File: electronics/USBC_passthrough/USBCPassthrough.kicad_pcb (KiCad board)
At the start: 4 copper layers, 41 x 14 mm, 2 parts, among them J1 USB_C_Receptacle_USB2.0_16P, J2 USB_C_Receptacle_USB2.0_16P

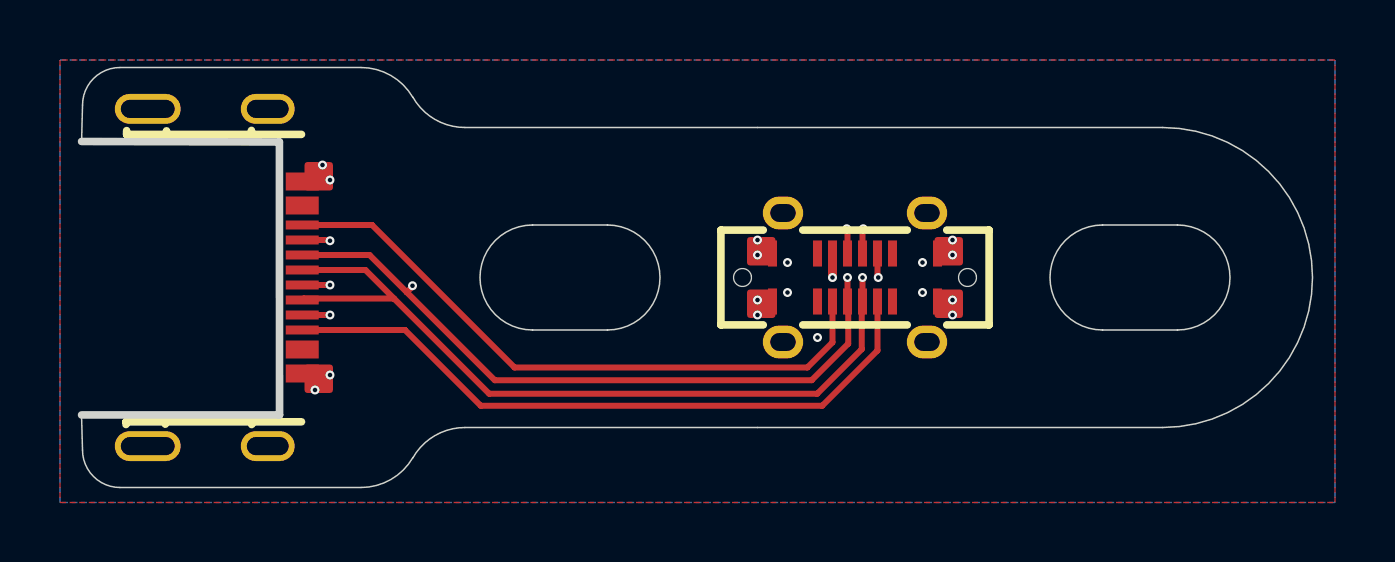
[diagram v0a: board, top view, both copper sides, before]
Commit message: fixed passthrough circuit
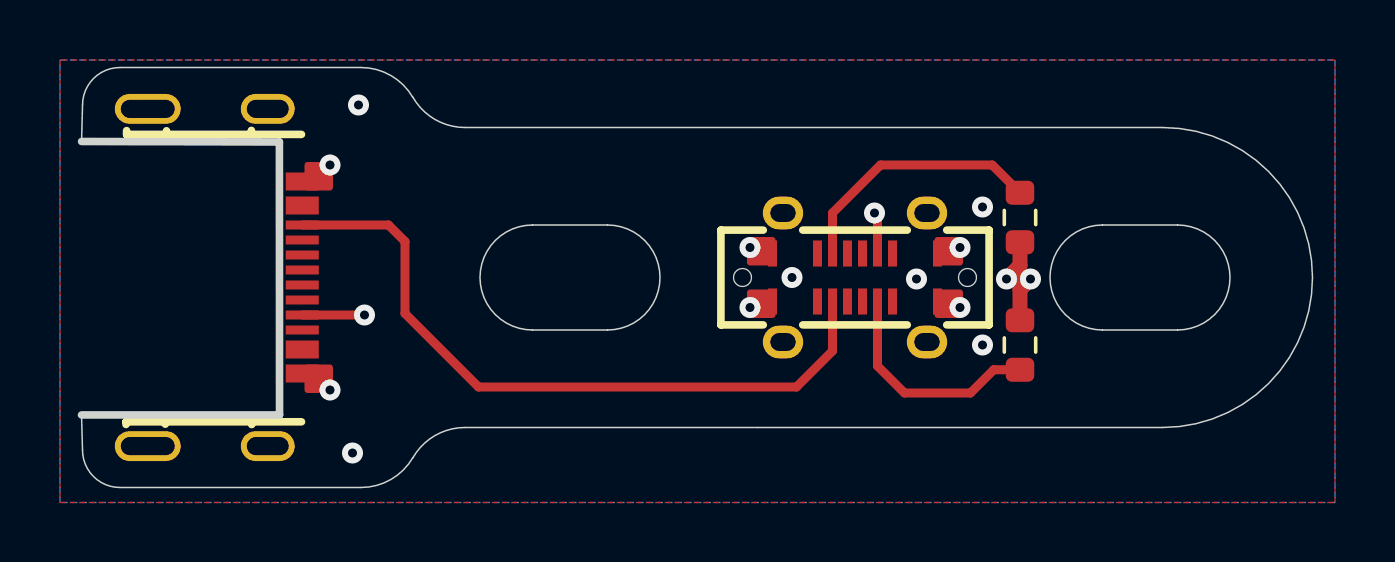
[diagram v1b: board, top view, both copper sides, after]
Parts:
- added R1: 5k1, Resistor_SMD:R_0603_1608Metric, F.Cu at (158.2, 97.0)
- added R2: 5k1, Resistor_SMD:R_0603_1608Metric, F.Cu at (158.2, 92.8)
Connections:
- J1 pad A6: Net-(J1-D+-PadA6) -> unconnected-(J1-D+-PadA6)
- J1 pad A7: Net-(J1-D--PadA7) -> unconnected-(J1-D--PadA7)
- J1 pad B6: Net-(J1-D+-PadA6) -> unconnected-(J1-D+-PadB6)
- J1 pad B7: Net-(J1-D--PadA7) -> unconnected-(J1-D--PadB7)
- J2 pad A5: Net-(J1-CC1) -> unconnected-(J2-CC1-PadA5)
- J2 pad A6: Net-(J1-D+-PadA6) -> unconnected-(J2-D+-PadA6)
- J2 pad A7: Net-(J1-D--PadA7) -> unconnected-(J2-D--PadA7)
- J2 pad B5: Net-(J1-CC2) -> unconnected-(J2-CC2-PadB5)
- J2 pad B6: Net-(J1-D+-PadA6) -> unconnected-(J2-D+-PadB6)
- J2 pad B7: Net-(J1-D--PadA7) -> unconnected-(J2-D--PadB7)
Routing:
- net Net-(J1-D--PadA7): track 29.4 -> 0.00 mm, vias 4 -> 0
- net Net-(J1-D+-PadA6): track 29.1 -> 0.00 mm, vias 2 -> 0
- net Net-(J1-CC1): track 23.7 -> 8.65 mm, vias 2 -> 0
- net Net-(J1-CC2): track 22.6 -> 7.59 mm
- net GND: track 0.00 -> 4.16 mm, vias 12 -> 8
- net Net-(J1-SBU1): track 24.0 -> 26.8 mm
- net Net-(J1-SBU2): track 21.4 -> 23.5 mm
- net +5V: vias 5 -> 6
